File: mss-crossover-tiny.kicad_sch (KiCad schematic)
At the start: 33 parts, among them J1 RJ45, J2 RJ45, J3 2x-screw, J4 2x-screw, J5 2x-screw, J6 ISP (5V), J7 Conn_01x10_Pin, J8 Conn_01x02_Pin, SW1 Set, U1 L78M05CDT, U2 LTV-355T, U3 ATtiny25-20SS, U4 ACS724xLCTR-05AB

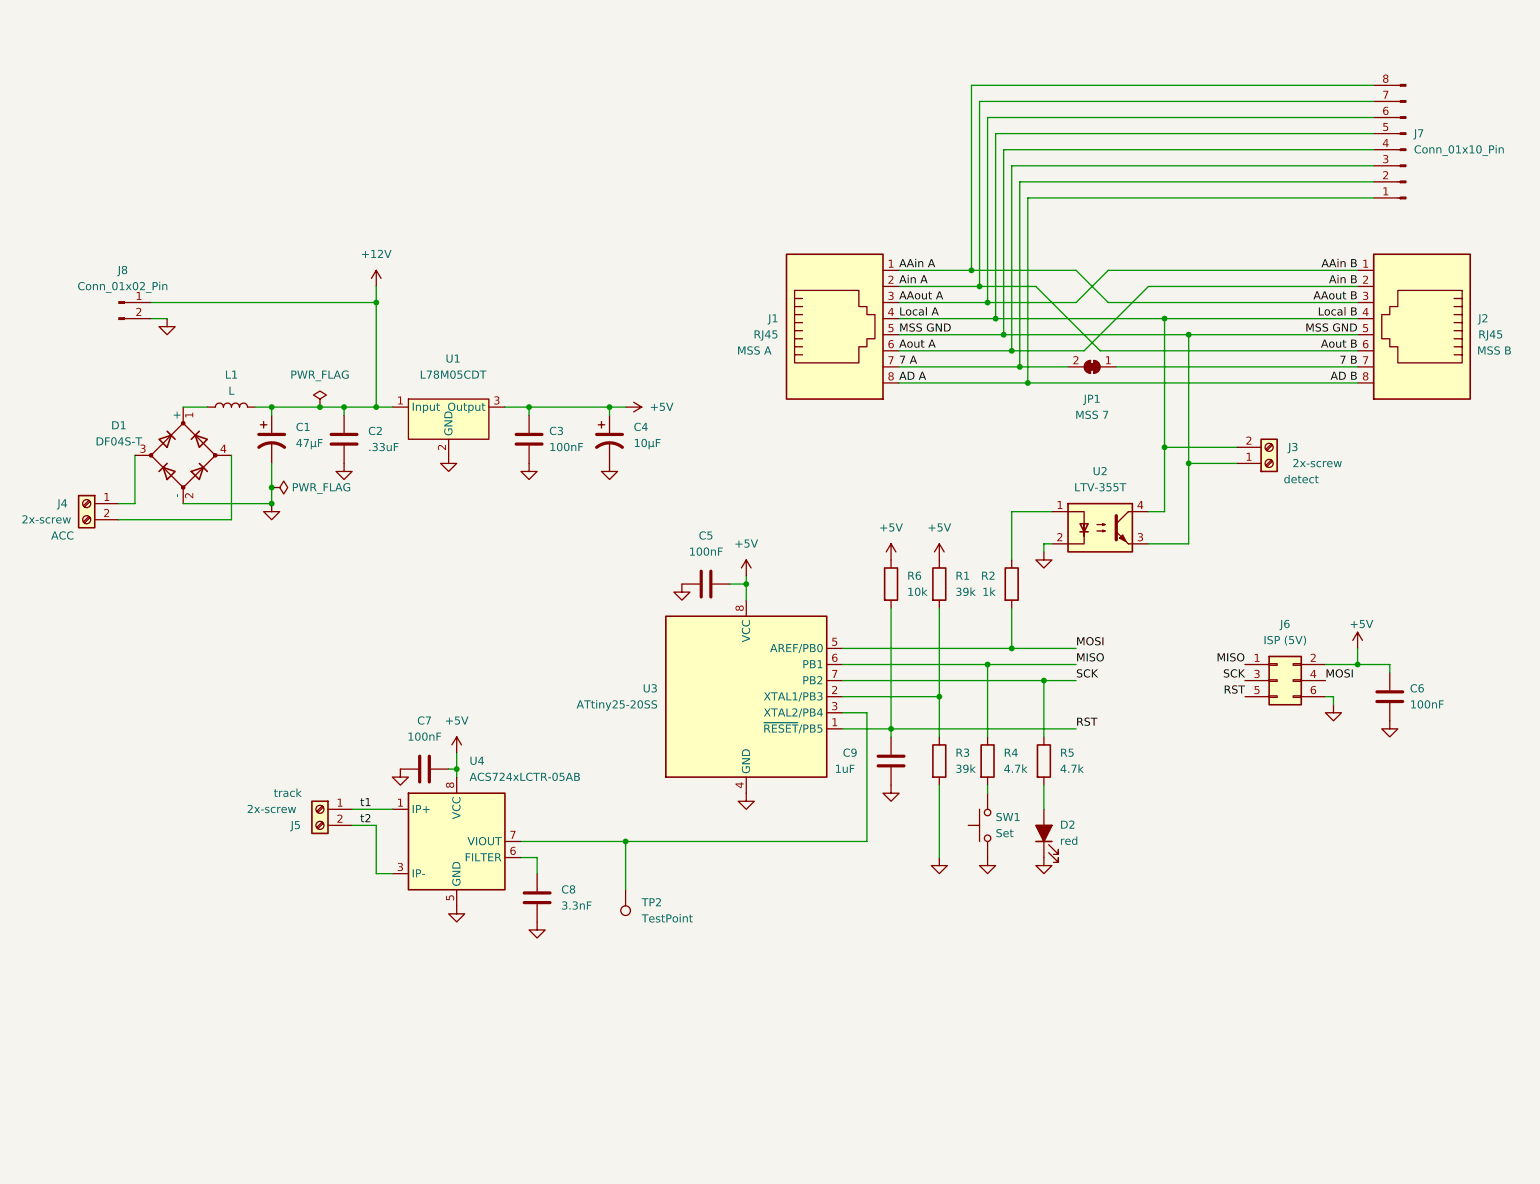
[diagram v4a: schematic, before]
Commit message: Little updates.  Moved power from 12V to ACC back to 12V.
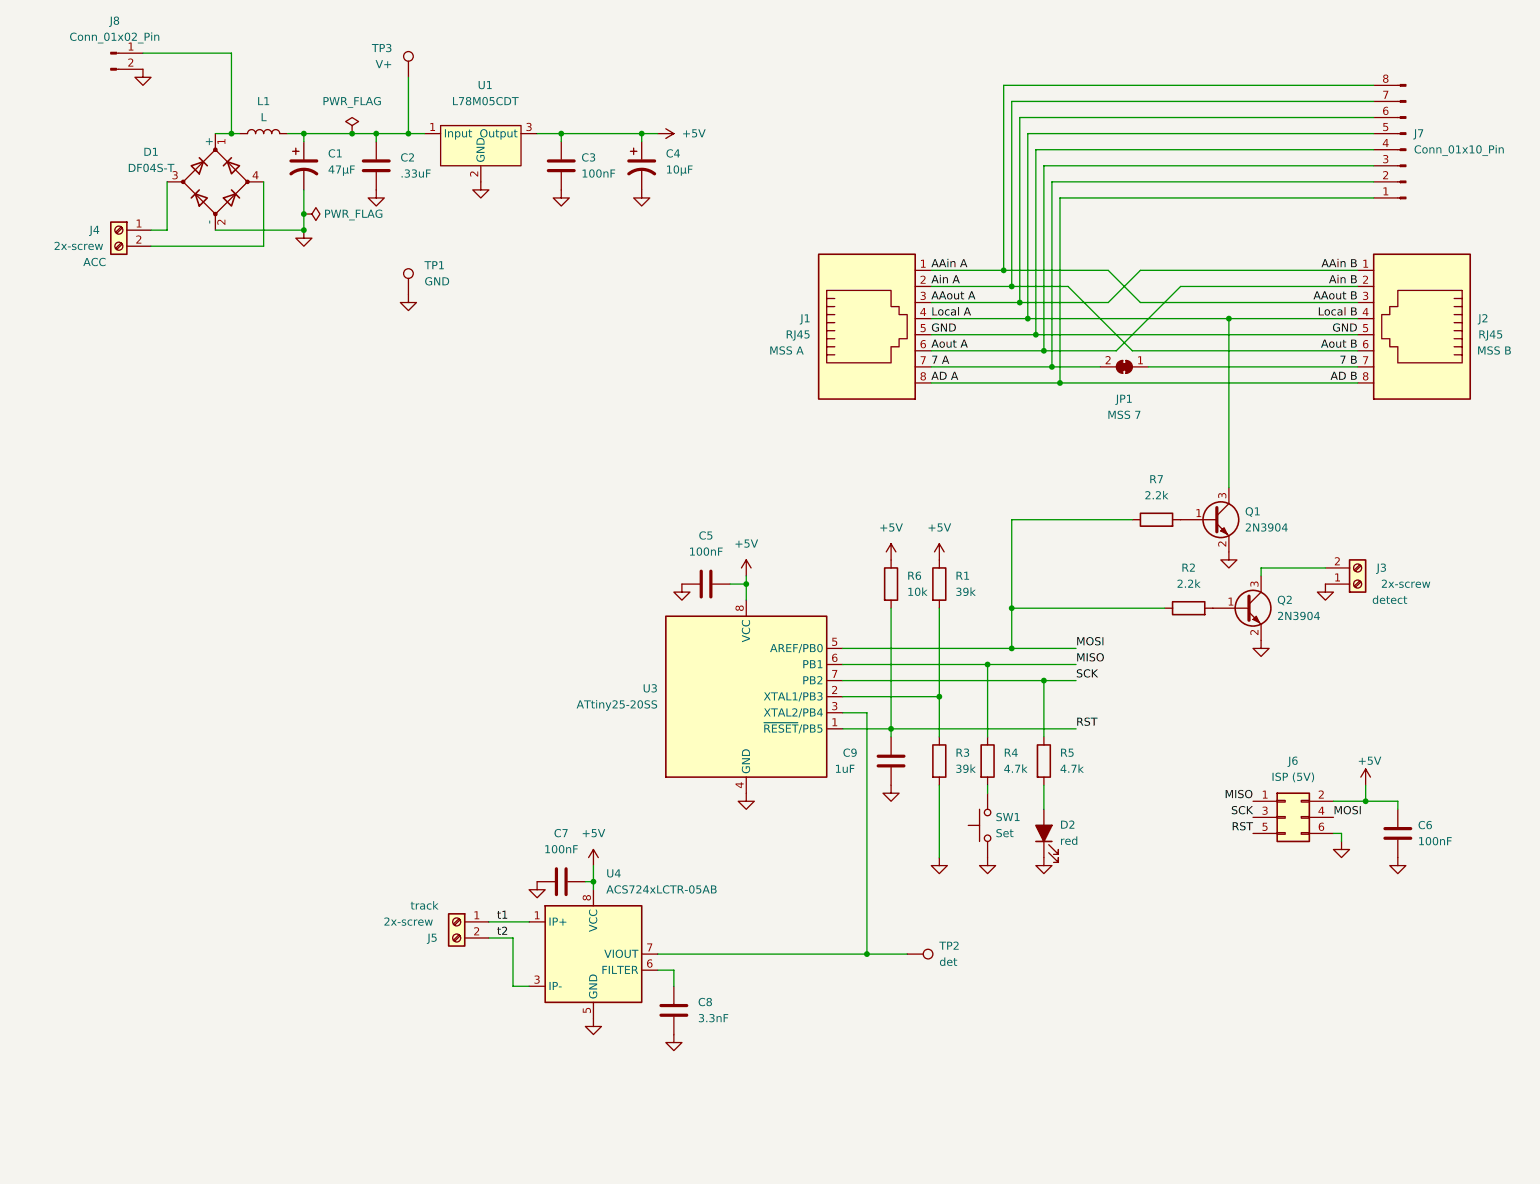
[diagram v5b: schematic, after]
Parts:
- removed U2: LTV-355T, myMods:LTV-355T, symbol Isolator:SFH617A-1
- added Q1, Q2: 2N3904, Package_TO_SOT_SMD:SOT-23, symbol Device:Q_NPN_BEC
- added R7: 2.2k, Resistor_SMD:R_0805_2012Metric_Pad1.20x1.40mm_HandSolder, symbol Device:R
- added TP1: GND, TestPoint:TestPoint_THTPad_1.5x1.5mm_Drill0.7mm, symbol Connector:TestPoint
- added TP3: V+, TestPoint:TestPoint_THTPad_1.5x1.5mm_Drill0.7mm, symbol Connector:TestPoint
- R2: value 1k -> 2.2k
- TP2: value TestPoint -> det; now left out of the parts list
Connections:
- net MSS GND is gone; now on net GND: J1.5, J2.5, J3.1 (Pin_1), J7.4 (Pin_4)
- net GND: now also Q1.2 (E), Q2.2 (E), TP1.1
- net Local A: now also Q1.3 (C); no longer J3.2 (Pin_2)
- net MOSI: now also R2.1, R7.1; no longer R2.2
- net at D1.1 (+), L1.1: now also J8.1 (Pin_1)
- net +12V: no longer names the net of C1.1, C2.1, L1.2, U1.1 (Input)
- net +12V: now also TP3.1; no longer J8.1 (Pin_1)
- new net: Q1.1 (B), R7.2
- new net: Q2.1 (B), R2.2
- new net: J3.2 (Pin_2), Q2.3 (C)
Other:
- moved on the sheet: C1, C2, C3, C4, C6, C7, C8, D1, J1, J3, J4, J5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

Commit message: Reworked design to use a current shunt instead.
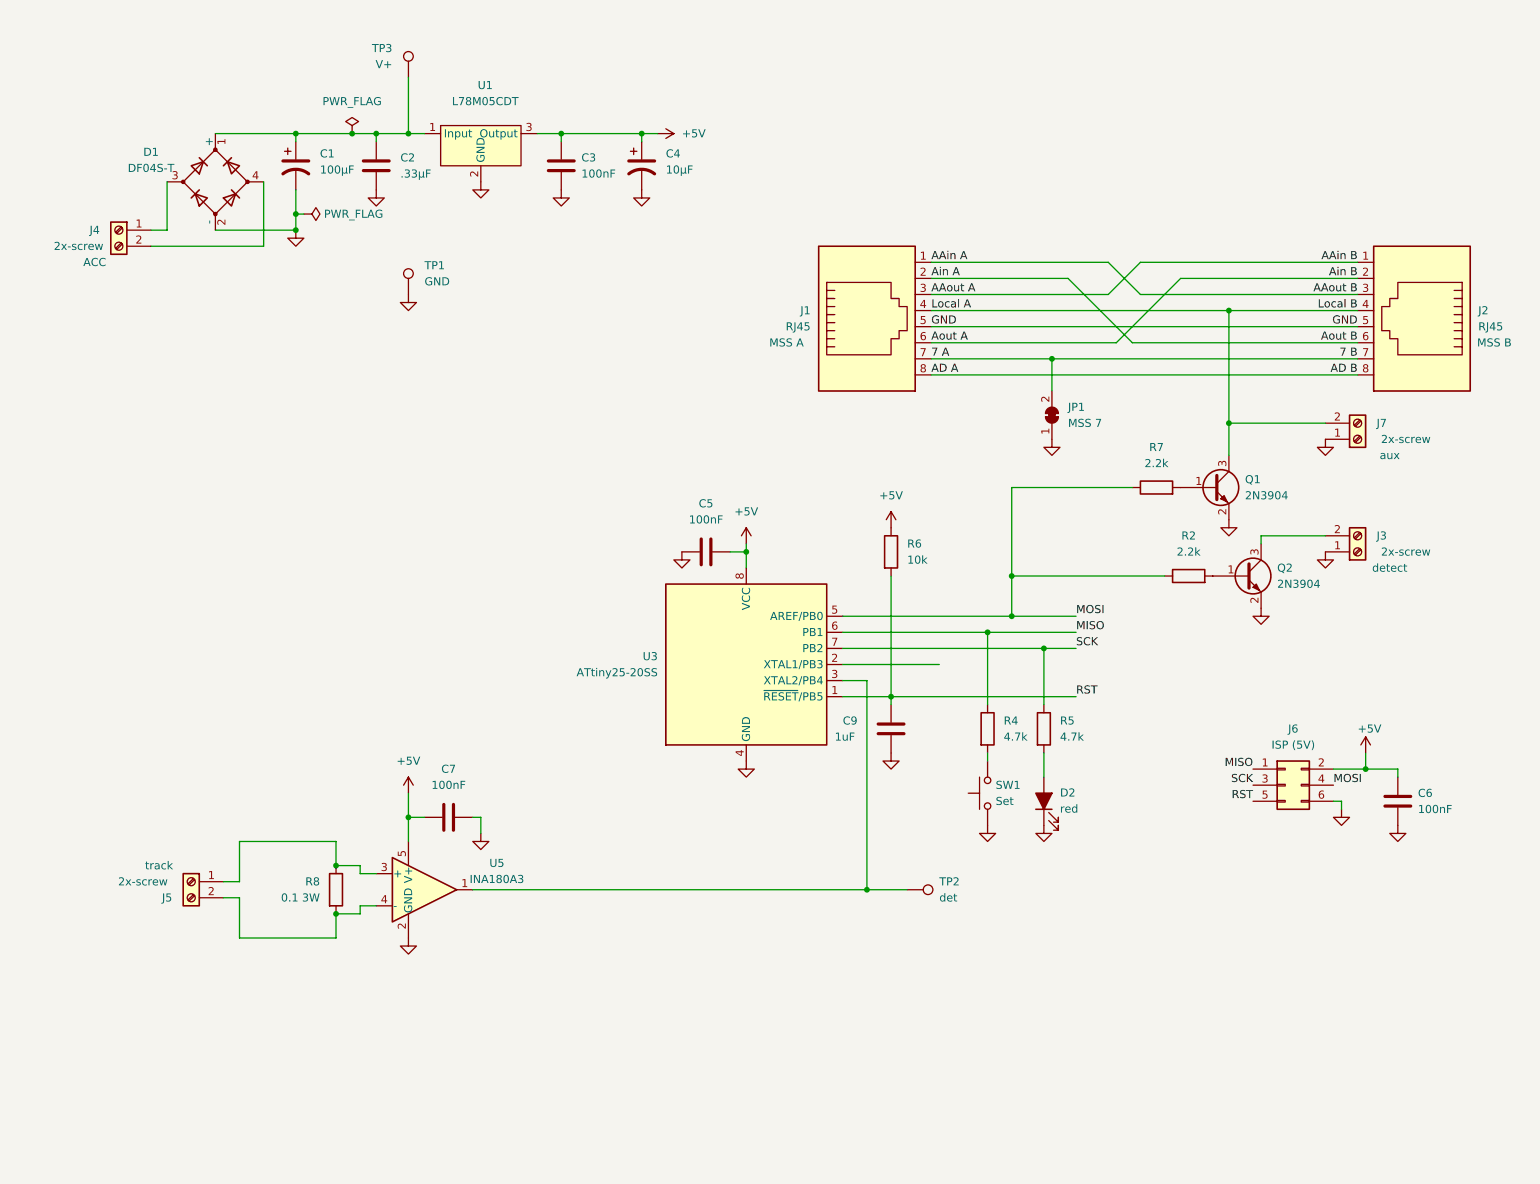
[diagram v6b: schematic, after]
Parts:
- removed C8: 3.3nF, Capacitor_SMD:C_0805_2012Metric_Pad1.18x1.45mm_HandSolder, symbol Device:C
- removed J7: Conn_01x10_Pin, Connector_PinHeader_2.00mm:PinHeader_1x08_P2.00mm_Vertical, symbol Connector:Conn_01x08_Pin
- removed J8: Conn_01x02_Pin, Connector_PinHeader_2.00mm:PinHeader_1x02_P2.00mm_Vertical, symbol Connector:Conn_01x02_Pin
- removed L1: L, Inductor_SMD:L_0805_2012Metric_Pad1.15x1.40mm_HandSolder, symbol Device:L
- removed R1, R3: 39k, Resistor_SMD:R_0805_2012Metric_Pad1.20x1.40mm_HandSolder, symbol Device:R
- removed U4: ACS724xLCTR-05AB, Package_SO:SOIC-8_3.9x4.9mm_P1.27mm, symbol Sensor_Current:ACS724xLCTR-05AB
- added J7: 2x-screw, Imports:CUI_TB003-500-P02BE, symbol Connector:Screw_Terminal_01x02
- added R8: 0.1 3W, Resistor_SMD:R_2512_6332Metric, symbol Device:R
- added U5: INA180A3, Package_TO_SOT_SMD:SOT-23-5, symbol Amplifier_Current:INA180A3
- C1: value 47µF -> 100µF; footprint Capacitor_SMD:CP_Elec_6.3x5.7 -> Capacitor_SMD:CP_Elec_6.3x7.7; MPN EEV476M035S9GAA -> EEV107M035A9HAA
- C2: value .33uF -> .33µF
- J1, J2: footprint Imports:CONN_RJSBE5080_16P13X12P57_AMP -> myMods:MJ3221-88; MPN RJHSE-5080 -> MJ3221-88
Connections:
- net +5V: now also C7.1, U5.5 (V+); no longer C7.2
- net 7 A: now also J2.7
- net GND: now also C7.2, JP1.1 (A), J7.1 (Pin_1), U5.2 (GND); no longer C7.1
- net Local A: now also J7.2 (Pin_2)
- net at C1.1, C2.1, TP3.1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: now also D1.1 (+)
- net at TP2.1, U3.3 (XTAL2/PB4): now also U5.1
- removed net 7 B: J2.7, JP1.1 (A)
- net t1: no longer names the net of J5.1 (Pin_1)
- net t1: now also R8.1, U5.3 (+)
- net t2: no longer names the net of J5.2 (Pin_2)
- net t2: now also R8.2, U5.4 (-)
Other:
- moved on the sheet: C1, C5, C6, C9, D2, J1, J2, J3, J5, J6, JP1, Q1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

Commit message: Still working on then redesign for a resistive sense element.  Also added optoisolators.
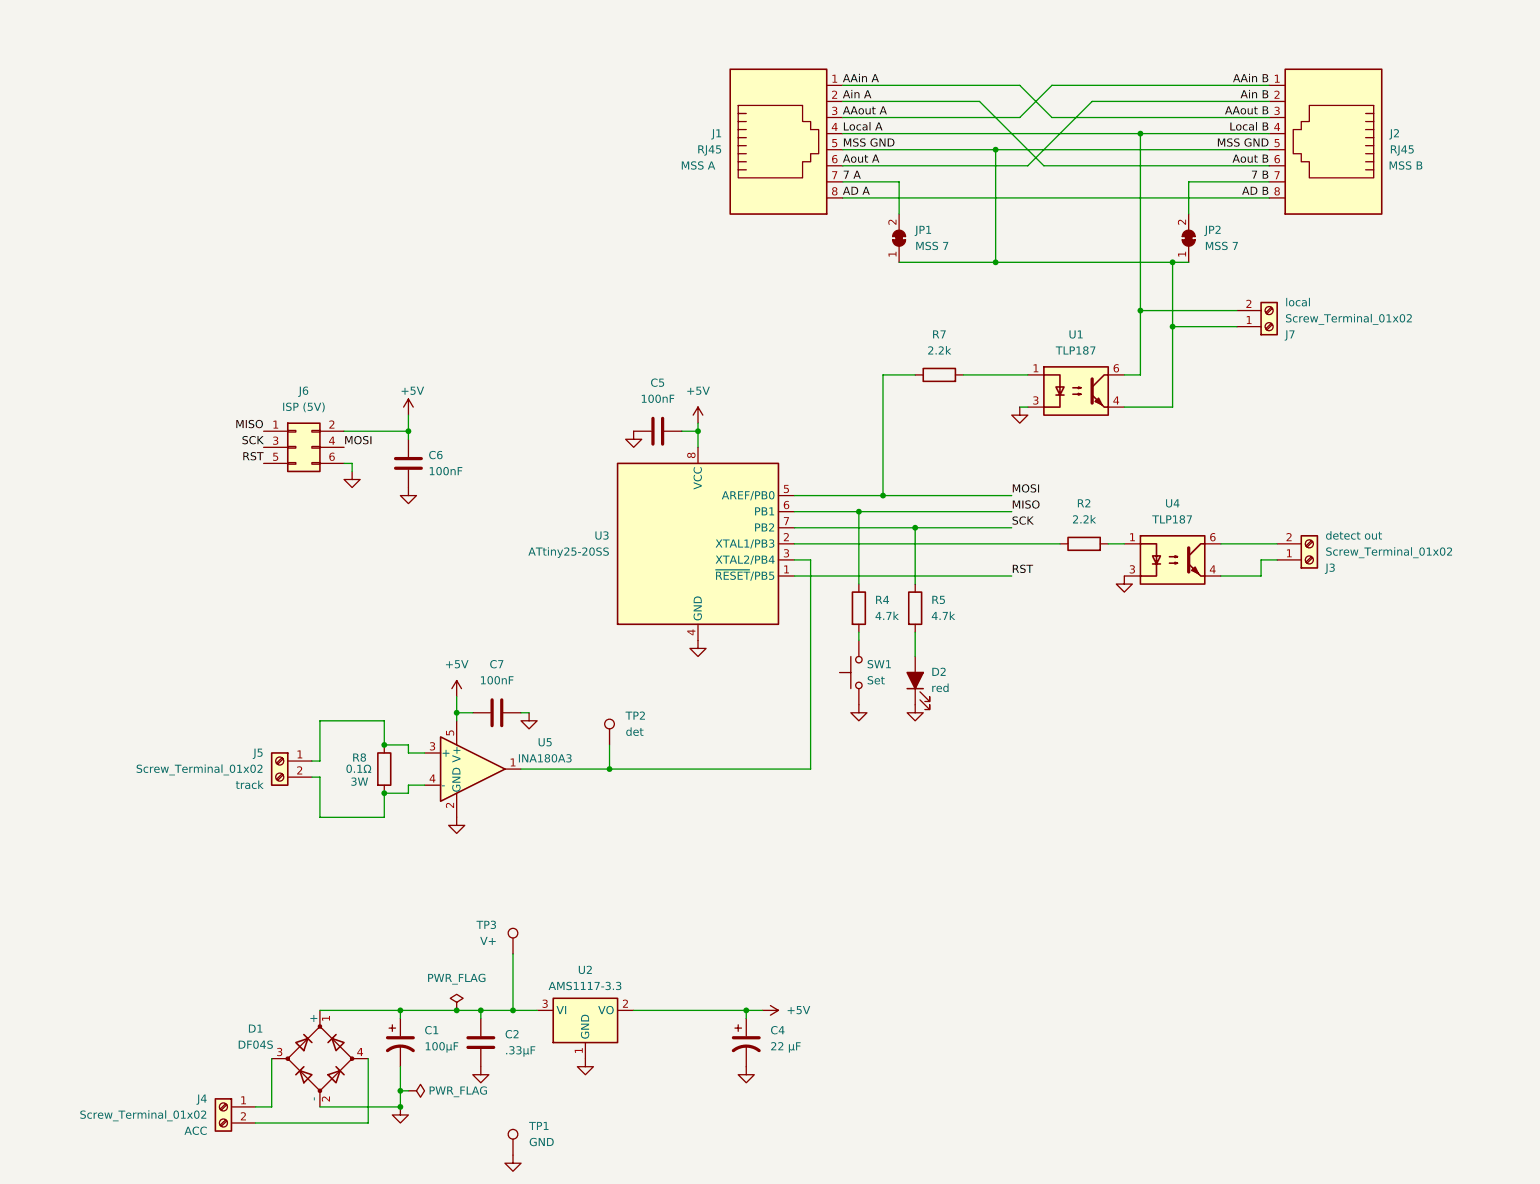
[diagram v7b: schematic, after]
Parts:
- removed C3: 100nF, Capacitor_SMD:C_0805_2012Metric_Pad1.18x1.45mm_HandSolder, symbol Device:C
- removed C9: 1uF, Capacitor_SMD:C_0805_2012Metric_Pad1.18x1.45mm_HandSolder, symbol Device:C
- removed Q1, Q2: 2N3904, Package_TO_SOT_SMD:SOT-23, symbol Device:Q_NPN_BEC
- removed R6: 10k, Resistor_SMD:R_0805_2012Metric_Pad1.20x1.40mm_HandSolder, symbol Device:R
- removed U1: L78M05CDT, Package_TO_SOT_SMD:TO-252-2, symbol myLib:L78M05CDT
- added JP2: MSS 7, Jumper:SolderJumper-2_P1.3mm_Bridged_RoundedPad1.0x1.5mm, symbol Jumper:SolderJumper_2_Bridged
- added U1, U4: TLP187, Package_SO:SOIC-4_4.55x3.7mm_P2.54mm, symbol Isolator:TLP185
- added U2: AMS1117-3.3, Package_TO_SOT_SMD:SOT-223-3_TabPin2, symbol Regulator_Linear:AMS1117-3.3
- C1: JLCPCB Part (none) -> C3338
- C2: JLCPCB Part (none) -> C1737
- C4: value 10µF -> 22 µF; footprint Capacitor_SMD:CP_Elec_4x5.7 -> Capacitor_Tantalum_SMD:CP_EIA-3216-18_Kemet-A_Pad1.58x1.35mm_HandSolder; FT Rotation Offset (none) -> 180; JLCPCB Part (none) -> C7183; MPN EEV106M035A9BAA -> (none)
- D1: value DF04S-T -> DF04S; FT Rotation Offset (none) -> 90; JLCPCB Part (none) -> C5185986; MPN DF04S-T -> DF04S
- D2: JLCPCB Part (none) -> C84256
- J1, J2: now left out of the parts list
- J3: value 2x-screw -> Screw_Terminal_01x02; footprint Imports:CUI_TB003-500-P02BE -> Imports:691210910002; Label detect -> detect out; MPN TB003-500-P02BE -> 691210910002; now left out of the parts list
- J4, J5: value 2x-screw -> Screw_Terminal_01x02; footprint Imports:CUI_TB003-500-P02BE -> Imports:691210910002; MPN TB003-500-P02BE -> 691210910002; now left out of the parts list
- J6: value ISP (5V) -> ISP (5V); footprint myMods:skedd-6-debugging -> Connector:Tag-Connect_TC2030-IDC-NL_2x03_P1.27mm_Vertical
- J7: value 2x-screw -> Screw_Terminal_01x02; footprint Imports:CUI_TB003-500-P02BE -> Imports:691210910002; Label aux -> local; MPN TB003-500-P02BE -> 691210910002; now left out of the parts list
- R8: value 0.1 3W -> 0.1Ω; JLCPCB Part (none) -> C7419997; Power (none) -> 3W
- SW1: FT Position Offset (none) -> 5,0; JLCPCB Part (none) -> C72443
- U5: MPN INA180A3IDBVR -> INA180A1IDBVR
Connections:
- net +5V: now also U2.2 (VO)
- net 7 A: no longer J2.7
- net GND: now also U1.3, U2.1 (GND), U4.3; no longer J1.5, J2.5, J3.1 (Pin_1), J7.1 (Pin_1), JP1.1 (A)
- net Local A: now also U1.6
- net MOSI: no longer R2.1
- net at R7.2: now also U1.1
- net at C1.1, C2.1, D1.1 (+)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: now also U2.3 (VI)
- net at R2.2: now also U4.1
- net at J3.2 (Pin_2): now also U4.6
- net at U3.2 (XTAL1/PB3): now also R2.1
- new net: J3.1 (Pin_1), U4.4
- new net 7 B: J2.7, JP2.2 (B)
- new net MSS GND: J1.5, J2.5, J7.1 (Pin_1), JP1.1 (A), JP2.1 (A), U1.4
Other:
- moved on the sheet: C1, C2, C4, C5, C6, C7, D1, D2, J1, J2, J6, JP1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
